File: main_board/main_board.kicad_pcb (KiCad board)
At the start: 2 copper layers, 61 parts, among them J1 CON-SMA-EDGE-S, J2 TSW-104-14-F-S, J3 TSW-104-14-F-S, U1 LT1722CS5-TRMPBF, U12 MIC5365-3.3YC5-TR, U2 TS5A4624DCKR, U3 AD5160, U4 TS5A4624DCKR, U5 AD8031ARTZ-REEL7, U6 LT1722CS5-TRMPBF, U7 LTC2315CTS8-12-PBF, U8 LT1818IS5-TRMPBF, U9 AP63205WU-7

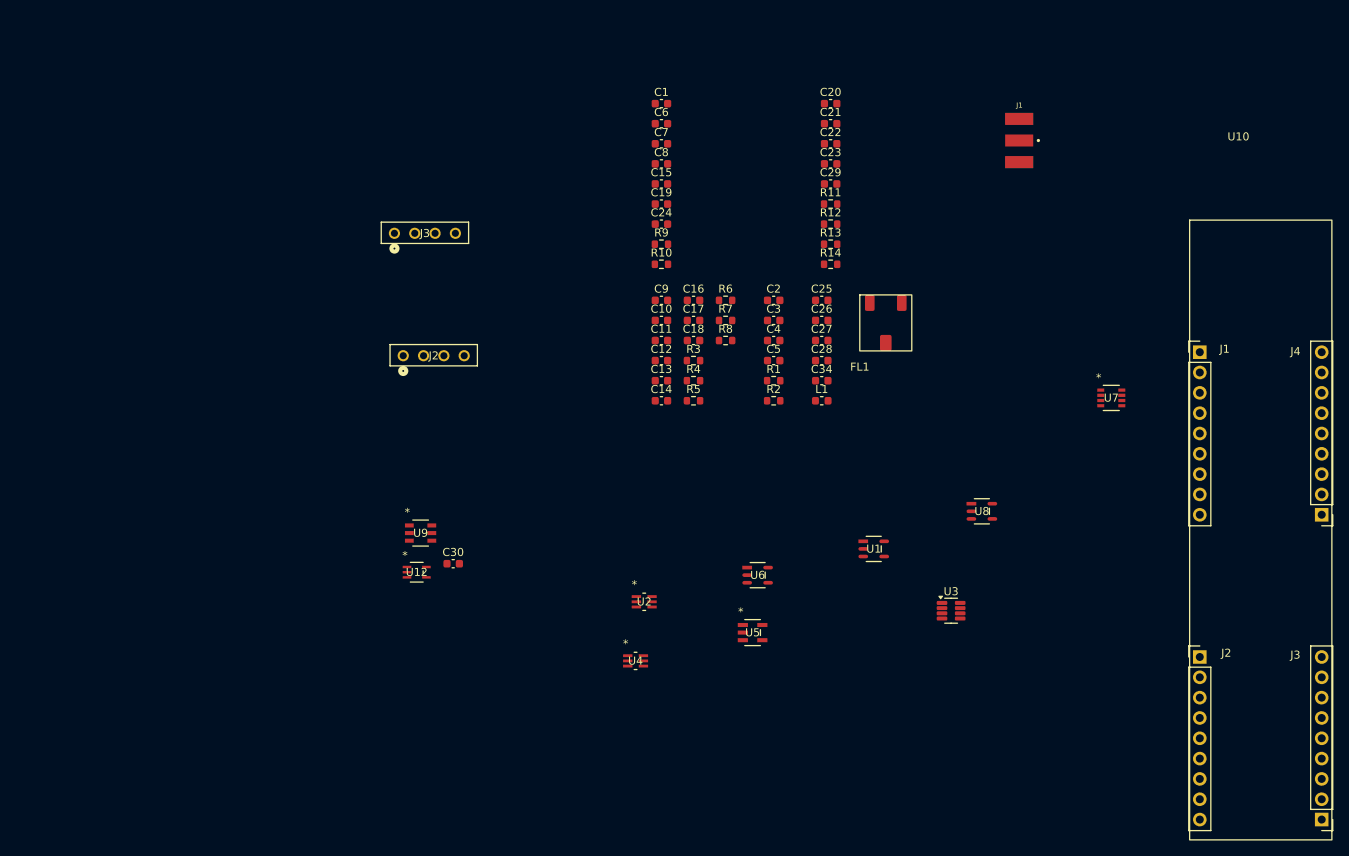
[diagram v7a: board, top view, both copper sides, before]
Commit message: Final Schematic is frozen, DO NOT MAKE CHANGES WITHOUT GROUP AGREEMENT. Also floorplan all major ICs on board.
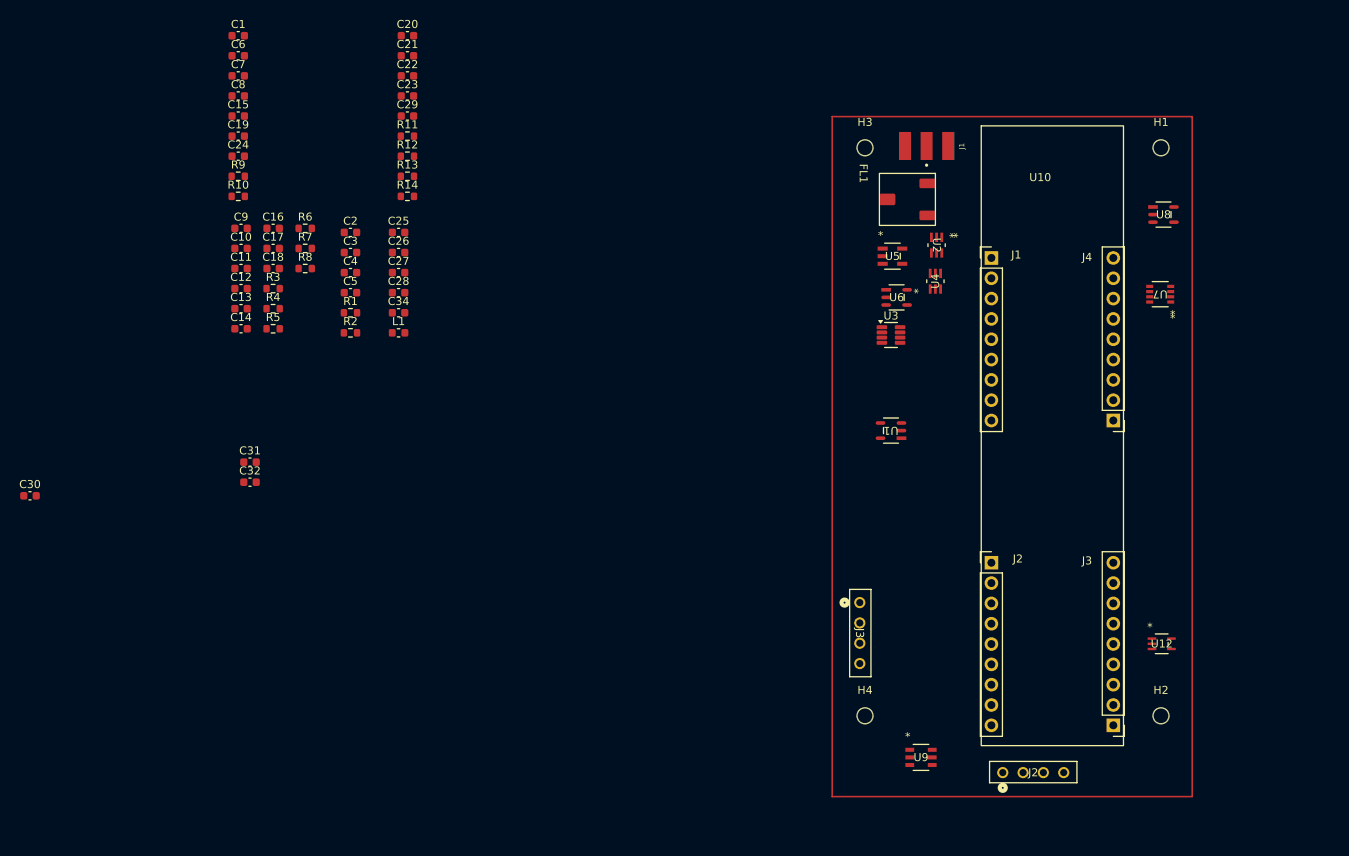
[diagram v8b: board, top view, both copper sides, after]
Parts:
- added C31: 10u, Capacitor_SMD:C_0603_1608Metric, F.Cu at (75.2, 108.7)
- added C32: 10u, Capacitor_SMD:C_0603_1608Metric, F.Cu at (75.2, 111.2)
- added H1: MountingHole, MountingHole:MountingHole_2mm, F.Cu at (189.1, 69.4)
- added H2: MountingHole, MountingHole:MountingHole_2mm, F.Cu at (189.1, 140.4)
- added H3: MountingHole, MountingHole:MountingHole_2mm, F.Cu at (152.1, 69.4)
- added H4: MountingHole, MountingHole:MountingHole_2mm, F.Cu at (152.1, 140.4)
- moved U12 93.5 mm to (189.2, 131.4)
- moved J2 91.3 mm to (173.1, 147.5)
- moved J3 73.8 mm to (151.4, 130.1), turned to -90 degrees
- moved U9 68.5 mm to (159.1, 145.6)
- moved U4 60.5 mm to (160.9, 86.1), turned to 90 degrees
- moved U2 57.6 mm to (161.1, 81.6), turned to -90 degrees
- moved C1 53.6 mm to (73.8, 55.4)
- moved C15 53.6 mm to (73.8, 65.4)
- moved C19 53.6 mm to (73.8, 68.0)
- moved C2 53.6 mm to (87.8, 80.0)
- moved C20 53.6 mm to (94.9, 55.4)
- moved C21 53.6 mm to (94.9, 57.9)
- moved C22 53.6 mm to (94.9, 60.4)
- moved C23 53.6 mm to (94.9, 62.9)
- moved C24 53.6 mm to (73.8, 70.5)
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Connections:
- U10 pad 19: unconnected-(U10-Pad19) -> /uart
- U10 pad 44: /Serial_Data_Out -> /CS_bar
- U10 pad 45: unconnected-(U10-Pad45) -> /SCK
- U10 pad 47: /SCK -> unconnected-(U10-Pad47)
- U10 pad 48: /CS_bar -> /Serial_Data_Out
- U10 pad 9: /uart -> unconnected-(U10-Pad9)
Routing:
- added copper zone on In2.Cu, net +5V
- added copper zone on In1.Cu, net GND
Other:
- copper layers 2 -> 4
